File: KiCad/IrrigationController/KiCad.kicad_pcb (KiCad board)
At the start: 2 copper layers, 100 x 100 mm, 130 parts, among them IC1 MCP23017-E_SO, IC2 MCP23017-E_SO, J1 Screw_Terminal_01x03, J10 Screw_Terminal_01x05, J11 Screw_Terminal_01x02, J12 Screw_Terminal_01x02, J13 Screw_Terminal_01x04, J14 Screw_Terminal_01x02, J15 Screw_Terminal_01x02, J16 Screw_Terminal_01x02, J17 Screw_Terminal_01x02, J18 Screw_Terminal_01x02, J19 Screw_Terminal_01x02, J2 Screw_Terminal_01x03, J3 Screw_Terminal_01x03, J4 Screw_Terminal_01x03, J5 Screw_Terminal_01x03, J6 Screw_Terminal_01x02, J7 Screw_Terminal_01x02, J8 Screw_Terminal_01x02, J9 Screw_Terminal_01x02, K1 2071556-9, K2 2071556-9, Q1 2N3906, Q10 2N3904, Q11 2N3904, Q12 2N3904, Q2 2N3906, Q3 2N3906, Q4 2N3906, Q5 2N3906, Q6 2N3904, Q7 2N3904, Q8 2N3904, Q9 2N3904, SW1 SW_Push, U1 L298HN, U2 ARDUINO_MKR_WAN_1310, U3 L298HN, U4 L298HN, U5 L298HN, U6 LM75AIMX_NOPB, U7 L7805

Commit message: BOMS
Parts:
- added D1: BAT54S, Package_TO_SOT_SMD:SOT-23, F.Cu at (309.4, 106.8)
- added D2: BAT54S, Package_TO_SOT_SMD:SOT-23, F.Cu at (309.4, 111.3)
- added D7: BAT54S, Package_TO_SOT_SMD:SOT-23, F.Cu at (309.4, 115.8)
- added IC3: DS89C21TMX_NOPB, SamacSys_Parts:SOIC127P600X175-8N, F.Cu at (316.1, 107.9)
- added J21: Screw_Terminal_01x06, TerminalBlock_Phoenix:TerminalBlock_Phoenix_MKDS-1,5-6_1x06_P5.00mm_Horizontal, F.Cu at (310.5, 99.0)
- added R7: PAD, Resistor_SMD:R_1206_3216Metric, F.Cu at (314.7, 112.8)
- C1, C10, C11, C12, C13, C14, C2, C3, C4, C5, C6, C7, C8, C9: footprint Capacitor_SMD:C_1206_3216Metric_Pad1.33x1.80mm_HandSolder -> Capacitor_SMD:C_1206_3216Metric
- D11, D12, D13, D14, D15, D16, D17, D18, D19, D20, D21, D22, D23, D24, D25, D26, D27, D28, D29, D30, D31, D32, D33, D34, D35, D36, D37, D38, D39, D40, D41, D42: value 1N4007 -> SS24; footprint Diode_SMD:D_1206_3216Metric_Pad1.42x1.75mm_HandSolder -> Diode_SMD:D_SMB
- Q1, Q2, Q3: value 2N3906 -> MMBT3906
- Q11, Q12, Q6, Q7, Q8: value 2N3904 -> MMBT3904
- R1, R3, R5: value 1.7k -> 1.8k; footprint Resistor_SMD:R_1206_3216Metric_Pad1.30x1.75mm_HandSolder -> Resistor_SMD:R_1206_3216Metric
- R11, R12, R13, R16, R17, R18, R2, R21, R22, R23, R26, R27, R28, R29, R30, R4, R6: footprint Resistor_SMD:R_1206_3216Metric_Pad1.30x1.75mm_HandSolder -> Resistor_SMD:R_1206_3216Metric
- U1, U3, U4, U5: value L298HN -> L298P
- U7: footprint Package_TO_SOT_THT:TO-220-3_Vertical -> Package_TO_SOT_SMD:TO-263-2
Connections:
- C14 pad 1: Net-(J19-Pin_2) -> +12V
- J19 pad 2: Net-(J19-Pin_2) -> +12V
- J5 pad 1: Net-(J5-Pin_1) -> +12V
- J5 pad 2: Net-(J5-Pin_2) -> /S_ANEM_IN
- R17 pad 2: +3V3 -> +3.3V
- R18 pad 2: +3V3 -> +3.3V
- U2 pad J3_12: /S_ILUM_EN -> unconnected-(U2-PA11/D3(PWM)-PadJ3_12)
- U2 pad J3_13: /S_ANEM_EN -> unconnected-(U2-PB10/D4(PWM)-PadJ3_13)
- U2 pad J3_5: /S_ILUM_IN -> unconnected-(U2-PA04/D18(PWM)/AIN(4)/A3-PadJ3_5)
- U2 pad J5_8: unconnected-(U2-PB23/D13/RX(SC5)-PadJ5_8) -> /RX
- U2 pad J5_9: unconnected-(U2-PB22/D14/TX(SC5)-PadJ5_9) -> /TX
- U7 pad 1: Net-(J19-Pin_2) -> +12V

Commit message: qwer
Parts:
- removed the D1 at (309.4, 106.8)
- removed the D1 at (114.6, 57.3)
- removed D10, D3, D4, D5, D6, D8, D9: 1N5711UR, Diode_SMD:D_1206_3216Metric_Pad1.42x1.75mm_HandSolder
- removed the D2 at (114.6, 60.7)
- removed the D2 at (309.4, 111.3)
- removed the D7 at (309.4, 115.8)
- removed the D7 at (18.6, 123.8)
- removed J4: Screw_Terminal_01x03, TerminalBlock_Phoenix:TerminalBlock_Phoenix_MKDS-1,5-3_1x03_P5.00mm_Horizontal
- removed Q10, Q9: 2N3904, Package_TO_SOT_SMD:SOT-23
- removed Q4, Q5: 2N3906, Package_TO_SOT_SMD:SOT-23
- removed R10, R8: 3.3k, Resistor_SMD:R_1206_3216Metric_Pad1.30x1.75mm_HandSolder
- removed R14, R15: 4.7k, Resistor_SMD:R_1206_3216Metric_Pad1.30x1.75mm_HandSolder
- removed R19, R20: 10k, Resistor_SMD:R_1206_3216Metric_Pad1.30x1.75mm_HandSolder
- removed R24, R25: 27k, Resistor_SMD:R_1206_3216Metric_Pad1.30x1.75mm_HandSolder
- removed the R7 at (27.7, 128.4)
- removed the R7 at (314.7, 112.8)
- removed R9: 1.7k, Resistor_SMD:R_1206_3216Metric_Pad1.30x1.75mm_HandSolder
- removed U6: LM75AIMX_NOPB, SamacSys_Parts:SOIC127P600X175-8N
- added C16: 100n, Capacitor_SMD:C_1206_3216Metric, F.Cu at (66.8, -1.57)
- added C17: 100n, Capacitor_SMD:C_1206_3216Metric, F.Cu at (66.8, 1.78)
- added C18: 100n, Capacitor_SMD:C_1206_3216Metric, F.Cu at (173.5, -22.1)
- added D1: BAT54S, Package_TO_SOT_SMD:SOT-23, F.Cu at (300.5, 139.0)
- added D2: BAT54S, Package_TO_SOT_SMD:SOT-23, F.Cu at (300.5, 143.6)
- added D7: BAT54S, Package_TO_SOT_SMD:SOT-23, F.Cu at (300.5, 148.3)
- added R7: PAD, Resistor_SMD:R_1206_3216Metric, F.Cu at (136.9, 168.4)
- added TP1: TestPoint, TestPoint:TestPoint_Pad_2.0x2.0mm, F.Cu at (303.0, 172.2)
- added TP2: TestPoint, TestPoint:TestPoint_Pad_2.0x2.0mm, F.Cu at (303.0, 176.3)
- C15: value 0.1u -> 100n; footprint Capacitor_SMD:C_1206_3216Metric_Pad1.33x1.80mm_HandSolder -> Capacitor_SMD:C_1206_3216Metric
- IC3: footprint SamacSys_Parts:SOIC127P600X175-8N -> SamacSys_Parts:SOP65P490X110-8N
- U1, U3, U4, U5: footprint Package_TO_SOT_THT:TO-220-15_P2.54x2.54mm_StaggerOdd_Lead4.58mm_Vertical -> Package_SO:HSOP-20-1EP_11.0x15.9mm_P1.27mm_SlugDown_ThermalVias
- moved Q7 277.6 mm to (305.4, 152.9)
- moved Q2 277.6 mm to (305.4, 139.0)
- moved U1 270.0 mm to (-38.6, 224.9)
- moved Q3 265.1 mm to (305.4, 143.6)
- moved Q8 264.2 mm to (310.3, 139.0)
- moved R22 245.8 mm to (268.0, 129.4)
- moved R17 244.0 mm to (262.4, 142.6)
- moved R3 242.0 mm to (256.7, 136.0)
- moved R4 242.0 mm to (256.7, 139.3)
- moved R12 239.2 mm to (262.4, 132.7)
- moved J3 239.0 mm to (257.5, 110.3)
- moved C3 239.0 mm to (1.48, 218.4)
- moved C1 239.0 mm to (1.48, 211.7)
- moved C2 239.0 mm to (1.48, 215.1)
- moved J2 238.6 mm to (257.5, 98.5)
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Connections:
- net /D0_1 renamed /D0+
- net /D0_2 renamed /D0-
- net /RI_1 renamed /RI+
- net /RI_2 renamed /RI-
- C15 pad 1: +5V -> Earth
- C15 pad 2: Earth -> /Vin
- U1 pad 10: /R1_IN2 -> Earth
- U1 pad 11: /R1_EN -> Earth
- U1 pad 12: /R1_IN1 -> +5V
- U1 pad 13: Net-(D13-A) -> /R1_IN2
- U1 pad 14: Net-(D11-A) -> /R1_EN
- U1 pad 15: Earth -> /R1_IN1
- U1 pad 2: Net-(D17-A) -> Earth
- U1 pad 3: Net-(D15-A) -> unconnected-(U1-NC-Pad3)
- U1 pad 4: +12V -> Net-(D17-A)
- U1 pad 5: /W2_IN2 -> Net-(D15-A)
- U1 pad 6: /W2_EN -> +12V
- U1 pad 7: /W2_IN1 -> /W2_IN2
- U1 pad 8: Earth -> /W2_EN
- U1 pad 9: +5V -> /W2_IN1
- U3 pad 10: /W1_IN2 -> Earth
- U3 pad 11: /W1_EN -> Earth
- U3 pad 12: /W1_IN1 -> +5V
- U3 pad 13: Net-(D21-A) -> /W1_IN2
- U3 pad 14: Net-(D19-A) -> /W1_EN
- U3 pad 15: Earth -> /W1_IN1
- U3 pad 2: Net-(D25-A) -> Earth
- U3 pad 3: Net-(D23-A) -> unconnected-(U3-NC-Pad3)
- U3 pad 4: +12V -> Net-(D25-A)
- U3 pad 5: /P5_IN2 -> Net-(D23-A)
- U3 pad 6: /P5_EN -> +12V
- U3 pad 7: /P5_IN1 -> /P5_IN2
- U3 pad 8: Earth -> /P5_EN
- U3 pad 9: +5V -> /P5_IN1
- U4 pad 10: /P4_IN2 -> Earth
- U4 pad 11: /P4_EN -> Earth
- U4 pad 12: /P4_IN1 -> +5V
- U4 pad 13: Net-(D29-A) -> /P4_IN2
- U4 pad 14: Net-(D27-A) -> /P4_EN
- U4 pad 15: Earth -> /P4_IN1
- U4 pad 2: Net-(D33-A) -> Earth
- U4 pad 3: Net-(D31-A) -> unconnected-(U4-NC-Pad3)
- U4 pad 4: +12V -> Net-(D33-A)
- U4 pad 5: /P3_IN2 -> Net-(D31-A)
- U4 pad 6: /P3_EN -> +12V
- U4 pad 7: /P3_IN1 -> /P3_IN2
- U4 pad 8: Earth -> /P3_EN
- U4 pad 9: +5V -> /P3_IN1
- U5 pad 10: /P2_IN2 -> Earth
- U5 pad 11: /P2_EN -> Earth
- U5 pad 12: /P2_IN1 -> +5V
- U5 pad 13: Net-(D37-A) -> /P2_IN2
- U5 pad 14: Net-(D35-A) -> /P2_EN
- U5 pad 15: Earth -> /P2_IN1
- U5 pad 2: Net-(D41-A) -> Earth
- U5 pad 3: Net-(D39-A) -> unconnected-(U5-NC-Pad3)
- U5 pad 4: +12V -> Net-(D41-A)
- U5 pad 5: /P1_IN2 -> Net-(D39-A)
- U5 pad 6: /P1_EN -> +12V
- U5 pad 7: /P1_IN1 -> /P1_IN2
- U5 pad 8: Earth -> /P1_EN
- U5 pad 9: +5V -> /P1_IN1
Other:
- board outline removed

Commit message: PCB created
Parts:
- moved Q1 253.6 mm to (80.3, 27.0)
- moved Q6 249.5 mm to (85.4, 30.5), turned to 180 degrees
- moved D7 244.9 mm to (82.8, 35.9), turned to 180 degrees
- moved Q2 244.6 mm to (80.4, 43.0)
- moved Q7 243.9 mm to (85.8, 46.7), turned to 180 degrees
- moved Q3 239.9 mm to (80.7, 59.7)
- moved Q8 237.0 mm to (85.6, 63.4), turned to 180 degrees
- moved D1 234.2 mm to (82.8, 52.7), turned to 180 degrees
- moved Q11 230.9 mm to (101.5, 103.8), turned to -90 degrees
- moved D2 230.2 mm to (82.8, 68.7), turned to 180 degrees
- moved R29 228.3 mm to (98.5, 103.5), turned to 90 degrees
- moved J16 227.5 mm to (98.5, 132.1)
- moved K1 222.1 mm to (96.7, 108.1), turned to -90 degrees
- moved J7 222.0 mm to (185.2, 119.7), turned to 90 degrees
- moved U1 216.4 mm to (152.7, 123.7), turned to -90 degrees
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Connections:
- J15 pad 1: /NO_1 -> /COM_1
- J15 pad 2: /COM_1 -> /NO_1
- J16 pad 1: /NO_2 -> /COM_2
- J16 pad 2: /COM_2 -> /NO_2
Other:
- board outline added: 125 x 120 mm

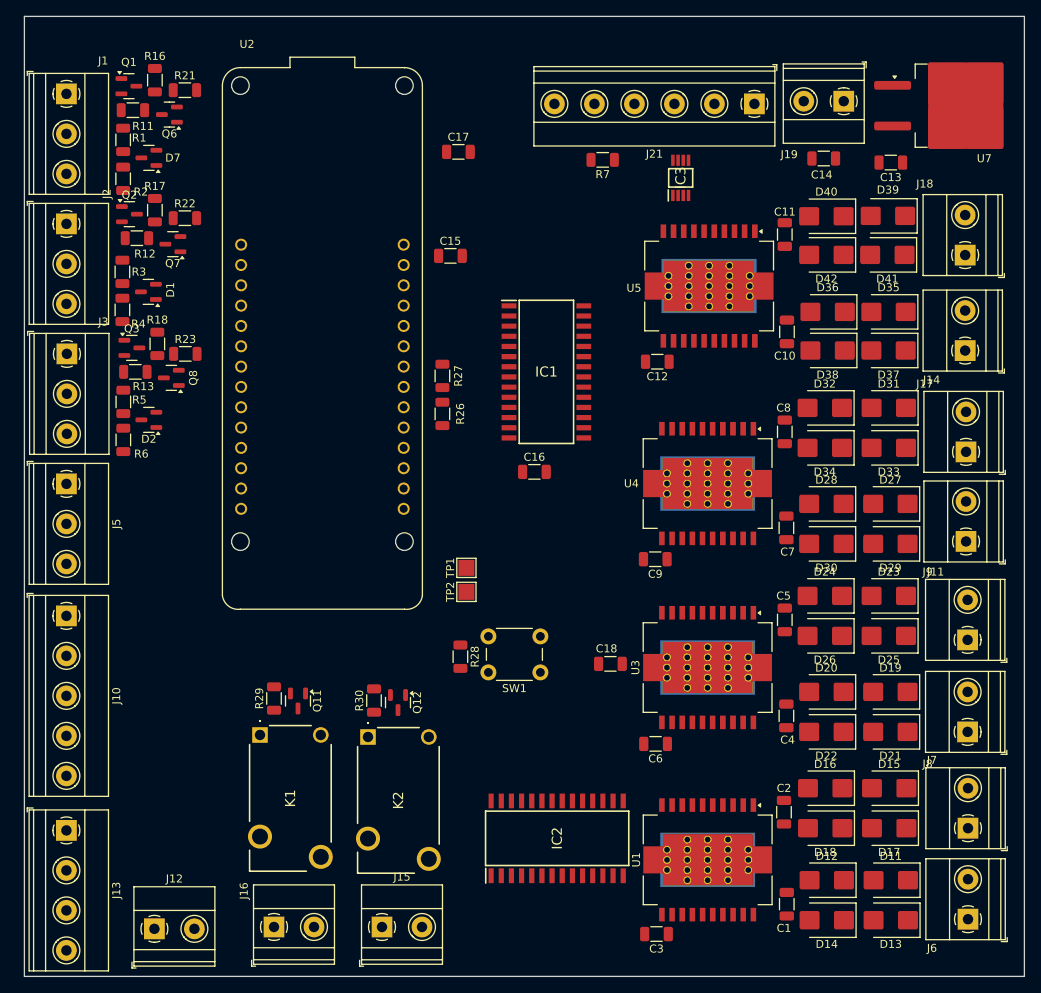
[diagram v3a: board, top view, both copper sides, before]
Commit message: L298 as Power
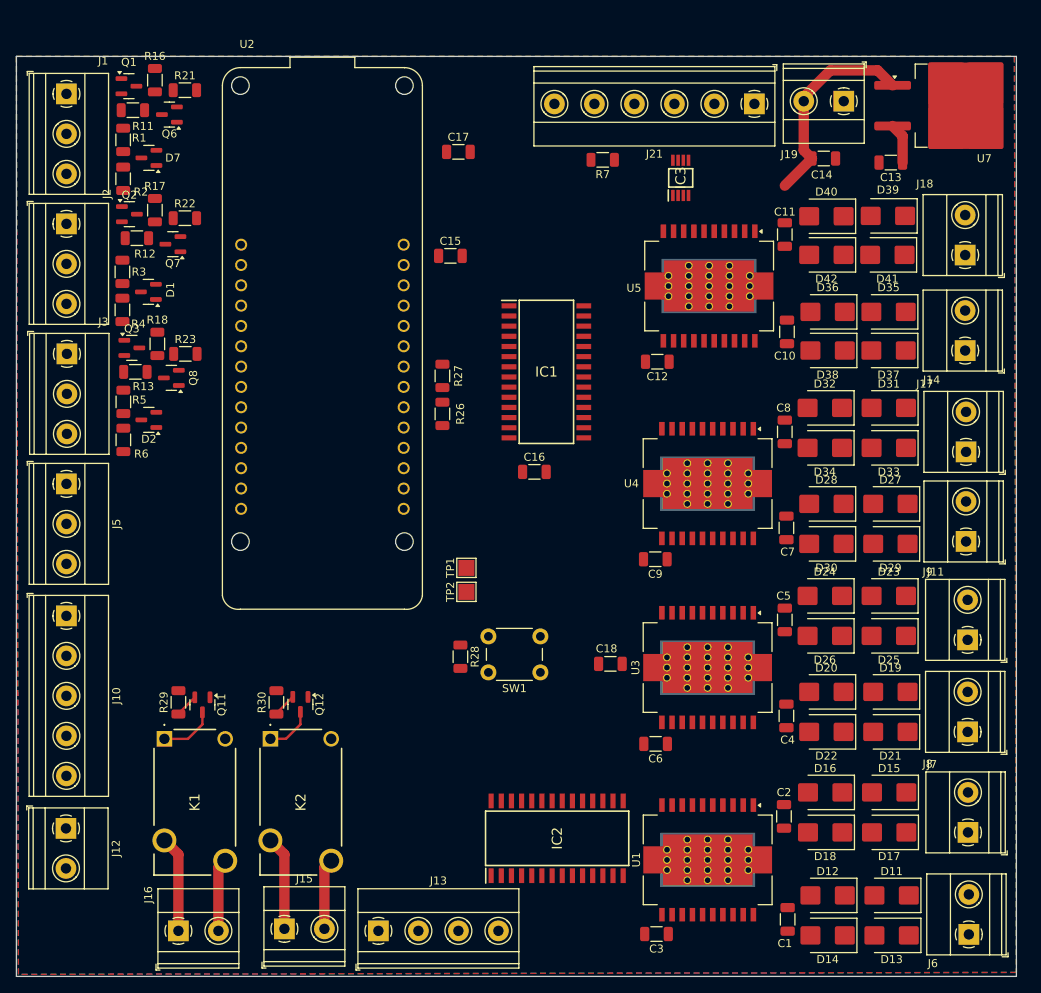
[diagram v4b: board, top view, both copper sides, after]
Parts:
- moved J13 41.0 mm to (111.5, 132.6), turned to 0 degrees
- moved J12 16.7 mm to (72.4, 119.8), turned to -90 degrees
- moved J15 12.2 mm to (99.8, 132.3)
- moved K2 12.2 mm to (98.0, 108.5)
- moved Q12 12.2 mm to (101.8, 104.2)
- moved R30 12.2 mm to (98.8, 104.0)
- moved J16 12.0 mm to (86.5, 132.6)
- moved K1 12.0 mm to (84.8, 108.6)
- moved Q11 12.0 mm to (89.5, 104.3)
- moved R29 12.0 mm to (86.5, 104.0)
- moved J6 1.90 mm to (185.3, 133.0)
- moved C1 1.90 mm to (162.7, 131.1)
- moved D13 1.90 mm to (175.7, 133.1)
- moved D14 1.90 mm to (167.7, 133.1)
- moved D11 1.90 mm to (175.7, 128.1)
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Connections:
- net Net-(D11-A) renamed /out_res_12
- net Net-(D13-A) renamed /out_res_11
- net Net-(D15-A) renamed /out_win_22
- net Net-(D19-A) renamed /out_win_12
- net Net-(D23-A) renamed /out_pump_52
- net Net-(D25-A) renamed /out_pump_51
- net Net-(D27-A) renamed /out_pump_42
- net Net-(D29-A) renamed /out_pump_41
- net Net-(D31-A) renamed /out_pump_32
- net Net-(D33-A) renamed /out_pump_31
- net Net-(D35-A) renamed /out_pump_22
- net Net-(D37-A) renamed /out_pump_21
- net Net-(D39-A) renamed /out_pump_12
- net Net-(D41-A) renamed /out_pump_11
- D17 pad 2: Net-(D17-A) -> /out_win_21
- D18 pad 1: Net-(D17-A) -> /out_win_21
- D21 pad 2: Net-(D21-A) -> /out_win_21
- D22 pad 1: Net-(D21-A) -> /out_win_21
- J7 pad 1: Net-(D17-A) -> /out_win_21
- J8 pad 1: Net-(D21-A) -> /out_win_21
- U1 pad 4: Net-(D17-A) -> /out_win_21
- U3 pad 16: Net-(D21-A) -> /out_win_21
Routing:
- net +12V: track 0.00 -> 26.2 mm
- net /COM_2: track 0.00 -> 12.0 mm
- net /COM_1: track 0.00 -> 11.8 mm
- net /NO_2: track 0.00 -> 9.11 mm
- net /NO_1: track 0.00 -> 8.87 mm
- net Net-(K1-COIL_1): track 0.00 -> 7.01 mm
- net Net-(K2-COIL_1): track 0.00 -> 6.06 mm
- net /Vin: track 0.00 -> 5.09 mm
- net Net-(Q12-B): track 0.00 -> 3.00 mm
- net Net-(Q11-B): track 0.00 -> 2.94 mm
- added copper zone on B.Cu, net +5V
- added copper zone on F.Cu, net Earth
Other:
- board size 125 x 120 mm -> 125 x 115 mm

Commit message: qwer
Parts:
- moved C17 11.7 mm to (119.8, 46.7)
- moved IC2 9.73 mm to (128.2, 113.0), turned to 180 degrees
- moved C15 1.42 mm to (119.8, 49.4), turned to 180 degrees
- turned C11 to 90 degrees
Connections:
- J10 pad 1: /FOCO_1_EN -> /FOCO_4_EN
- J10 pad 2: /FOCO_2_EN -> /FOCO_3_EN
- J10 pad 3: /FOCO_3_EN -> /FOCO_2_EN
- J10 pad 4: /FOCO_4_EN -> /FOCO_1_EN
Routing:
- net /out_win_21: track 0.00 -> 87.2 mm, vias 0 -> 4
- net /out_win_12: track 0.00 -> 45.6 mm, vias 0 -> 2
- net /out_pump_51: track 0.00 -> 45.5 mm, vias 0 -> 2
- net /out_res_11: track 0.00 -> 44.2 mm, vias 0 -> 2
- net /out_res_12: track 0.00 -> 44.1 mm, vias 0 -> 2
- net /out_pump_52: track 0.00 -> 44.1 mm, vias 0 -> 2
- net /out_pump_11: track 0.00 -> 44.0 mm, vias 0 -> 2
- net /out_pump_32: track 0.00 -> 43.6 mm, vias 0 -> 2
- net /out_pump_31: track 0.00 -> 43.6 mm, vias 0 -> 2
- net /out_pump_12: track 0.00 -> 43.4 mm, vias 0 -> 2
- net /out_pump_21: track 0.00 -> 43.0 mm, vias 0 -> 2
- net /out_pump_42: track 0.00 -> 43.0 mm, vias 0 -> 2
- net /out_win_22: track 0.00 -> 42.8 mm, vias 0 -> 2
- net /out_pump_41: track 0.00 -> 41.8 mm, vias 0 -> 2
- net Earth: track 0.00 -> 28.7 mm
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- removed copper zone on B.Cu, net +5V
- removed copper zone on F.Cu, net Earth

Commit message: tracing in controller
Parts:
- removed TP1, TP2: TestPoint, TestPoint:TestPoint_Pad_2.0x2.0mm
- added J4: Conn_01x04_Pin, Connector_PinHeader_2.54mm:PinHeader_1x04_P2.54mm_Vertical, F.Cu at (122.9, 40.4)
- moved C17 66.3 mm to (122.8, 113.0), turned to -90 degrees
- moved C18 56.4 mm to (119.7, 46.8)
- moved IC3 19.7 mm to (129.7, 36.5), turned to 0 degrees
- moved R28 17.5 mm to (122.0, 80.8), turned to 180 degrees
- moved SW1 15.5 mm to (120.0, 90.2), turned to 90 degrees
- moved J15 13.4 mm to (86.4, 132.4)
- moved J16 13.4 mm to (99.9, 132.4)
- moved K1 13.4 mm to (84.6, 108.7)
- moved K2 13.4 mm to (98.1, 108.4)
- moved Q11 13.4 mm to (102.9, 104.2)
- moved Q12 13.4 mm to (88.4, 104.4)
- moved R29 13.4 mm to (99.9, 103.9)
- moved R30 13.4 mm to (85.4, 104.1)
- moved C16 9.52 mm to (123.6, 69.2), turned to -90 degrees
- moved IC2 3.84 mm to (130.6, 110.0), turned to 0 degrees
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- renumbered K2 to K1, K1 to K2
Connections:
- C16 pad 1: +5V -> +3.3V
- C17 pad 1: +5V -> +3.3V
- IC1 pad 21: /P3_IN2 -> /P5_EN
- IC1 pad 25: /P5_EN -> /P3_EN
- IC1 pad 26: /P5_IN1 -> /P3_IN1
- IC1 pad 27: /P5_IN2 -> /P3_IN2
- IC1 pad 7: /P3_EN -> /P5_IN1
- IC1 pad 8: /P3_IN1 -> /P5_IN2
- IC2 pad 21: /W1_EN -> /W2_EN
- IC2 pad 22: /W1_IN1 -> /W2_IN1
- IC2 pad 23: /W1_IN2 -> /W2_IN2
- IC2 pad 24: /W2_EN -> /W1_EN
- IC2 pad 25: /W2_IN1 -> /W1_IN1
- IC2 pad 26: /W2_IN2 -> /W1_IN2
- IC2 pad 27: /RELAY_2_EN -> unconnected-(IC2-GPA6-Pad27)
- IC2 pad 28: /RELAY_1_EN -> unconnected-(IC2-GPA7-Pad28)
- IC2 pad 7: unconnected-(IC2-GPB6-Pad7) -> /RELAY_1_EN
- IC2 pad 8: unconnected-(IC2-GPB7-Pad8) -> /RELAY_2_EN
- U2 pad J3_13: unconnected-(U2-PB10/D4(PWM)-PadJ3_13) -> /PULSE_IN
- U2 pad J3_7: /PULSE_IN -> unconnected-(U2-PA06/D20/AIN(6)/A5-PadJ3_7)
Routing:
- net +12V: track 21.8 -> 528.5 mm, vias 0 -> 11
- net Earth: track 28.7 -> 332.3 mm, vias 0 -> 20
- net +3.3V: track 0.00 -> 190.4 mm, vias 0 -> 12
- net /SDA: track 0.00 -> 89.8 mm, vias 0 -> 2
- net /SCL: track 0.00 -> 89.0 mm, vias 0 -> 4
- net +5V: track 12.3 -> 95.5 mm, vias 0 -> 12
- net /Vin: track 8.75 -> 70.9 mm, vias 0 -> 2
- net /FOCO_1_EN: track 0.00 -> 58.1 mm, vias 0 -> 2
- net /HEAT_EN: track 0.00 -> 58.1 mm, vias 0 -> 2
- net /FOCO_2_EN: track 0.00 -> 57.1 mm, vias 0 -> 2
- net /FOCO_3_EN: track 0.00 -> 56.0 mm, vias 0 -> 2
- net /FOCO_4_EN: track 0.00 -> 55.2 mm, vias 0 -> 2
- net /RELAY_1_EN: track 0.00 -> 47.7 mm
- net /S_HUM_1_EN: track 0.00 -> 44.8 mm
- net /R1_EN: track 0.00 -> 44.2 mm, vias 0 -> 2
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- added copper zone on F.Cu, net +12V
- added copper zone on F.Cu, net +5V
- added copper zone on B.Cu, net Earth
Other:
- board size 125 x 115 mm -> 121.5 x 115 mm
- board text added: "5+"
- board text added: "Anem"
- board text added: "GND"
- board text added: "Heat"
- board text added: "Hum 1"
- board text added: "Light"
- board text added: "RX"
- board text added: "TX"

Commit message: qwer
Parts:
- moved Q2 0.60 mm to (80.4, 43.6)
- moved R12 0.60 mm to (81.0, 46.6)
- moved R2 0.15 mm to (79.6, 38.4)
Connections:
- D21 pad 2: /out_win_21 -> /out_win_11
- D22 pad 1: /out_win_21 -> /out_win_11
- J8 pad 1: /out_win_21 -> /out_win_11
- U3 pad 16: /out_win_21 -> /out_win_11
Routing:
- net /out_win_21: track 87.2 -> 44.6 mm, vias 4 -> 2
- net /out_win_11: track 0.00 -> 42.6 mm, vias 0 -> 2
- net /out_pump_22: track 27.9 -> 44.0 mm

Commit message: pcb rev1
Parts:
- removed J4: Conn_01x04_Pin, Connector_PinHeader_2.54mm:PinHeader_1x04_P2.54mm_Vertical
- moved SW1 65.4 mm to (124.3, 24.9), turned to -90 degrees
- moved R28 46.6 mm to (122.4, 34.2), turned to 0 degrees
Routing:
- net /PULSE_IN: track 37.9 -> 9.56 mm, vias 1 -> 0
- net +3.3V: track 190.4 -> 201.3 mm, vias 12 -> 11
- net +5V: track 95.5 -> 88.1 mm, vias 12 -> 11
- net Earth: track 332.2 -> 329.3 mm, vias 20 -> 23
- net +12V: track 528.5 -> 526.8 mm, vias 11 -> 10
- net /RX: track 40.4 -> 38.9 mm
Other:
- board text removed: "5+"
- board text removed: "RX"
- board text removed: "TX"
